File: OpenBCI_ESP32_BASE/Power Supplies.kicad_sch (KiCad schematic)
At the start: 32 parts, among them J1 Conn_01x02, J2 Conn_02x03_Odd_Even, J3 Conn_02x02_Odd_Even, SW1 SW_SPDT, U10 TPS72325, U8 TPS60403, U9 TPS73225

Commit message: Firmware updates
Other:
- moved on the sheet: C33
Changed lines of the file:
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@@
   (junction (at 72.39 91.44) (diameter 0) (color 0 0 0 0)
   )
-  (junction (at 27.94 58.42) (diameter 0) (color 0 0 0 0)
+  (junction (at 21.59 58.42) (diameter 0) (color 0 0 0 0)
   )
   (junction (at 110.49 104.14) (diameter 0) (color 0 0 0 0)
@@
     (stroke (width 0) (type default) (color 0 0 0 0))
   )
-  (wire (pts (xy 27.94 58.42) (xy 27.94 62.23))
+  (wire (pts (xy 21.59 58.42) (xy 21.59 62.23))
     (stroke (width 0) (type default) (color 0 0 0 0))
   )
@@
     (stroke (width 0) (type default) (color 0 0 0 0))
   )
-  (wire (pts (xy 27.94 58.42) (xy 38.1 58.42))
-    (stroke (width 0) (type default) (color 0 0 0 0))
-  )
   (wire (pts (xy 75.565 170.18) (xy 81.28 170.18))
     (stroke (width 0) (type default) (color 0 0 0 0))
@@
     (stroke (width 0) (type default) (color 0 0 0 0))
   )
-  (wire (pts (xy 27.94 52.07) (xy 27.94 58.42))
+  (wire (pts (xy 21.59 52.07) (xy 21.59 58.42))
     (stroke (width 0) (type default) (color 0 0 0 0))
   )
@@
     (stroke (width 0) (type default) (color 0 0 0 0))
   )
+  (wire (pts (xy 21.59 58.42) (xy 38.1 58.42))
+    (stroke (width 0) (type default) (color 0 0 0 0))
+  )
   (wire (pts (xy 80.01 132.08) (xy 80.01 128.27))
     (stroke (width 0) (type default) (color 0 0 0 0))
@@
     (stroke (width 0) (type default) (color 0 0 0 0))
   )
-  (wire (pts (xy 27.94 74.93) (xy 27.94 69.85))
+  (wire (pts (xy 21.59 74.93) (xy 21.59 69.85))
     (stroke (width 0) (type default) (color 0 0 0 0))
   )
@@
     (pin "5")
   )
-  (symbol (lib_id "Device:C") (at 27.94 66.04 0) (unit 1)
-    (in_bom yes) (on_board yes)
-    (property "Reference" "C33" (id 0) (at 30.861 64.8716 0)
-      (effects (font (size 1.27 1.27)) (justify left))
-    )
-    (property "Value" "10u" (id 1) (at 30.861 67.183 0)
-      (effects (font (size 1.27 1.27)) (justify left))
-    )
-    (property "Footprint" "Capacitor_SMD:C_0805_2012Metric" (id 2) (at 28.9052 69.85 0)
-      (effects (font (size 1.27 1.27)) hide)
-    )
-    (property "Datasheet" "~" (id 3) (at 27.94 66.04 0)
+  (symbol (lib_id "Device:C") (at 21.59 66.04 0) (unit 1)
+    (in_bom yes) (on_board yes)
+    (property "Reference" "C33" (id 0) (at 24.511 64.8716 0)
+      (effects (font (size 1.27 1.27)) (justify left))
+    )
+    (property "Value" "10u" (id 1) (at 24.511 67.183 0)
+      (effects (font (size 1.27 1.27)) (justify left))
+    )
+    (property "Footprint" "Capacitor_SMD:C_0805_2012Metric" (id 2) (at 22.5552 69.85 0)
+      (effects (font (size 1.27 1.27)) hide)
+    )
+    (property "Datasheet" "~" (id 3) (at 21.59 66.04 0)
       (effects (font (size 1.27 1.27)) hide)
     )
@@
     (pin "2")
   )
-  (symbol (lib_id "power:+5V") (at 27.94 52.07 0) (unit 1)
-    (in_bom yes) (on_board yes)
-    (property "Reference" "#PWR023" (id 0) (at 27.94 55.88 0)
-      (effects (font (size 1.27 1.27)) hide)
-    )
-    (property "Value" "+5V" (id 1) (at 28.321 47.6758 0))
-    (property "Footprint" "" (id 2) (at 27.94 52.07 0)
-      (effects (font (size 1.27 1.27)) hide)
-    )
-    (property "Datasheet" "" (id 3) (at 27.94 52.07 0)
+  (symbol (lib_id "power:+5V") (at 21.59 52.07 0) (unit 1)
+    (in_bom yes) (on_board yes)
+    (property "Reference" "#PWR023" (id 0) (at 21.59 55.88 0)
+      (effects (font (size 1.27 1.27)) hide)
+    )
+    (property "Value" "+5V" (id 1) (at 21.971 47.6758 0))
+    (property "Footprint" "" (id 2) (at 21.59 52.07 0)
+      (effects (font (size 1.27 1.27)) hide)
+    )
+    (property "Datasheet" "" (id 3) (at 21.59 52.07 0)
       (effects (font (size 1.27 1.27)) hide)
     )
@@
     (pin "6")
   )
-  (symbol (lib_id "power:GND") (at 27.94 74.93 0) (unit 1)
-    (in_bom yes) (on_board yes)
-    (property "Reference" "#PWR024" (id 0) (at 27.94 81.28 0)
-      (effects (font (size 1.27 1.27)) hide)
-    )
-    (property "Value" "GND" (id 1) (at 28.067 79.3242 0))
-    (property "Footprint" "" (id 2) (at 27.94 74.93 0)
-      (effects (font (size 1.27 1.27)) hide)
-    )
-    (property "Datasheet" "" (id 3) (at 27.94 74.93 0)
-      (effects (font (size 1.27 1.27)) hide)
-    )
+  (symbol (lib_id "power:GND") (at 21.59 74.93 0) (unit 1)
+    (in_bom yes) (on_board yes)
+    (property "Reference" "#PWR024" (id 0) (at 21.59 81.28 0)
+      (effects (font (size 1.27 1.27)) hide)
+    )
+    (property "Value" "GND" (id 1) (at 21.717 79.3242 0))
+    (property "Footprint" "" (id 2) (at 21.59 74.93 0)
+      (effects (font (size 1.27 1.27)) hide)
+    )
+    (property "Datasheet" "" (id 3) (at 21.59 74.93 0)
+      (effects (font (size 1.27 1.27)) hide)
+    )

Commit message: Code and STL updates
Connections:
- net +2V5: now also J2.2 (Pin_2), J2.4 (Pin_4); no longer J2.1 (Pin_1), J2.3 (Pin_3)
- net -2V5: now also J3.2 (Pin_2), J3.4 (Pin_4); no longer J3.1 (Pin_1), J3.3 (Pin_3)
- net GND: now also J2.1 (Pin_1), J2.3 (Pin_3), J2.5 (Pin_5), J3.1 (Pin_1), J3.3 (Pin_3); no longer J2.2 (Pin_2), J2.4 (Pin_4), J2.6 (Pin_6), J3.2 (Pin_2), J3.4 (Pin_4)
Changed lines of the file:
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@@
 (kicad_sch (version 20211123) (generator eeschema)
   (paper "A4")
+  (junction (at 207.01 128.27) (diameter 0) (color 0 0 0 0)
+  )
   (junction (at 124.46 58.42) (diameter 0) (color 0 0 0 0)
   )
@@
   )
   (junction (at 72.39 128.27) (diameter 0) (color 0 0 0 0)
-  )
-  (junction (at 207.01 128.27) (diameter 0) (color 0 0 0 0)
   )
   (junction (at 166.37 128.27) (diameter 0) (color 0 0 0 0)
@@
     (stroke (width 0) (type default) (color 0 0 0 0))
   )
+  (wire (pts (xy 223.52 128.27) (xy 226.06 128.27))
+    (stroke (width 0) (type default) (color 0 0 0 0))
+  )
   (wire (pts (xy 223.52 91.44) (xy 226.06 91.44))
     (stroke (width 0) (type default) (color 0 0 0 0))
@@
     (stroke (width 0) (type default) (color 0 0 0 0))
   )
-  (wire (pts (xy 223.52 128.27) (xy 226.06 128.27))
-    (stroke (width 0) (type default) (color 0 0 0 0))
-  )
   (wire (pts (xy 81.28 91.44) (xy 72.39 91.44))
     (stroke (width 0) (type default) (color 0 0 0 0))
@@
     (stroke (width 0) (type default) (color 0 0 0 0))
   )
-  (wire (pts (xy 210.82 128.27) (xy 207.01 128.27))
-    (stroke (width 0) (type default) (color 0 0 0 0))
-  )
   (wire (pts (xy 109.855 167.64) (xy 109.855 166.37))
     (stroke (width 0) (type default) (color 0 0 0 0))
@@
   )
   (wire (pts (xy 72.39 130.81) (xy 72.39 128.27))
+    (stroke (width 0) (type default) (color 0 0 0 0))
+  )
+  (wire (pts (xy 207.01 128.27) (xy 210.82 128.27))
     (stroke (width 0) (type default) (color 0 0 0 0))
   )
@@
     (pin "1")
   )
-  (symbol (lib_id "Connector_Generic:Conn_02x02_Odd_Even") (at 215.9 128.27 0) (unit 1)
+  (symbol (lib_id "Connector_Generic:Conn_02x02_Odd_Even") (at 218.44 128.27 0) (mirror y) (unit 1)
     (in_bom yes) (on_board yes)
     (property "Reference" "J3" (id 0) (at 217.17 122.7582 0))
     (property "Value" "Conn_02x02_Odd_Even" (id 1) (at 217.17 125.0696 0))
-    (property "Footprint" "OpenBCI_ESP32:PinHeaderReverse_2x02_P2.54mml_OpenBCI" (id 2) (at 215.9 128.27 0)
-      (effects (font (size 1.27 1.27)) hide)
-    )
-    (property "Datasheet" "~" (id 3) (at 215.9 128.27 0)
+    (property "Footprint" "OpenBCI_ESP32:PinHeaderReverse_2x02_P2.54mml_OpenBCI" (id 2) (at 218.44 128.27 0)
+      (effects (font (size 1.27 1.27)) hide)
+    )
+    (property "Datasheet" "~" (id 3) (at 218.44 128.27 0)
       (effects (font (size 1.27 1.27)) hide)
     )
@@
     (pin "1")
   )
-  (symbol (lib_id "Connector_Generic:Conn_02x03_Odd_Even") (at 215.9 93.98 0) (unit 1)
+  (symbol (lib_id "Connector_Generic:Conn_02x03_Odd_Even") (at 218.44 93.98 0) (mirror y) (unit 1)
     (in_bom yes) (on_board yes)
     (property "Reference" "J2" (id 0) (at 217.17 85.9282 0))
     (property "Value" "Conn_02x03_Odd_Even" (id 1) (at 217.17 88.2396 0))
-    (property "Footprint" "OpenBCI_ESP32:PinHeaderReverse_2x03_P2.54mm_OpenBCI" (id 2) (at 215.9 93.98 0)
-      (effects (font (size 1.27 1.27)) hide)
-    )
-    (property "Datasheet" "~" (id 3) (at 215.9 93.98 0)
-      (effects (font (size 1.27 1.27)) hide)
-    )
+    (property "Footprint" "OpenBCI_ESP32:PinHeaderReverse_2x03_P2.54mm_OpenBCI" (id 2) (at 218.44 93.98 0)
+      (effects (font (size 1.27 1.27)) hide)
+    )
+    (property "Datasheet" "~" (id 3) (at 218.44 93.98 0)
+      (effects (font (size 1.27 1.27)) hide)
+    )

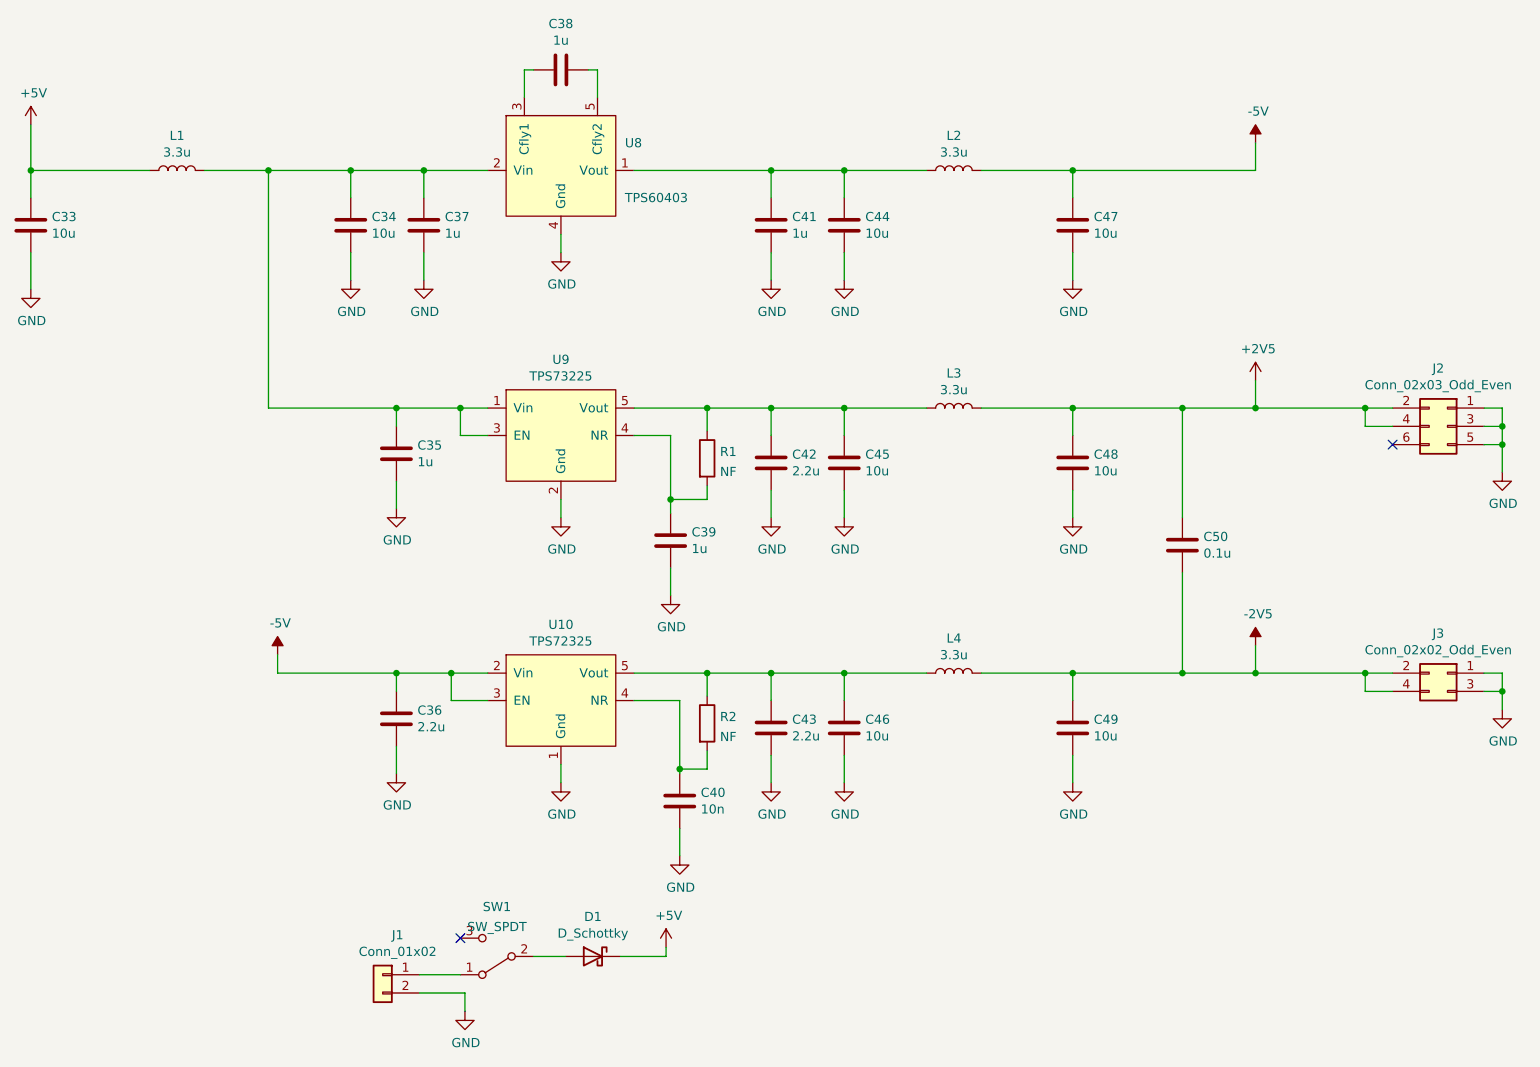
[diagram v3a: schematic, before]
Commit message: add ADS1298 files
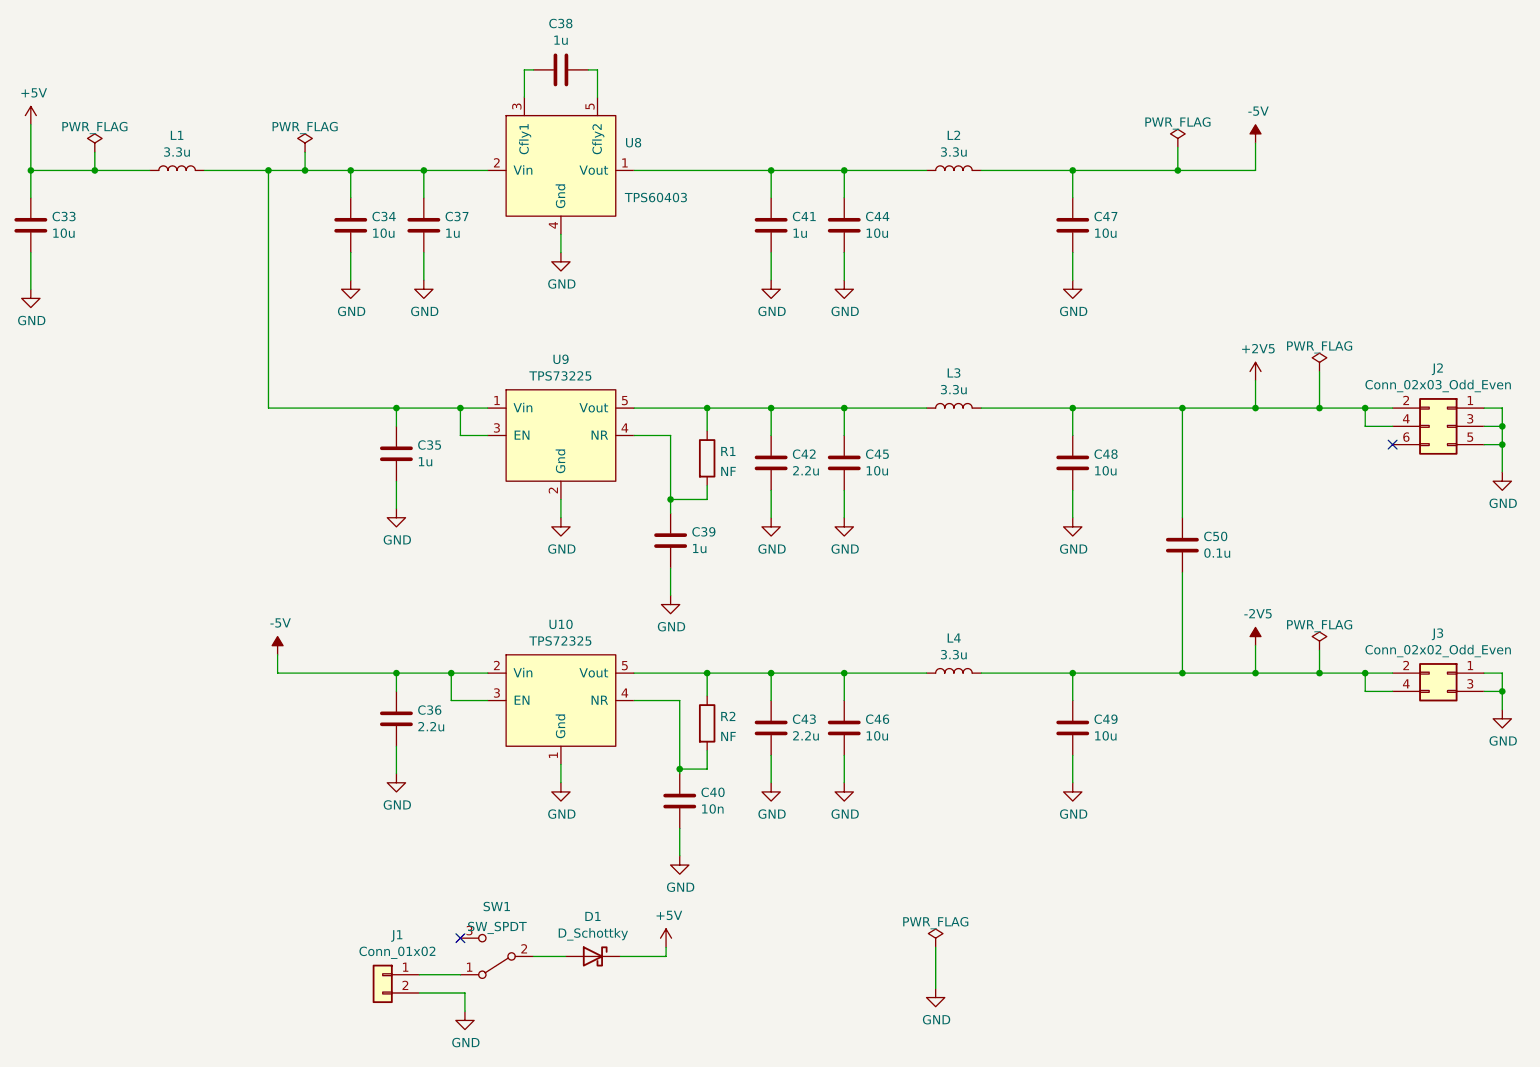
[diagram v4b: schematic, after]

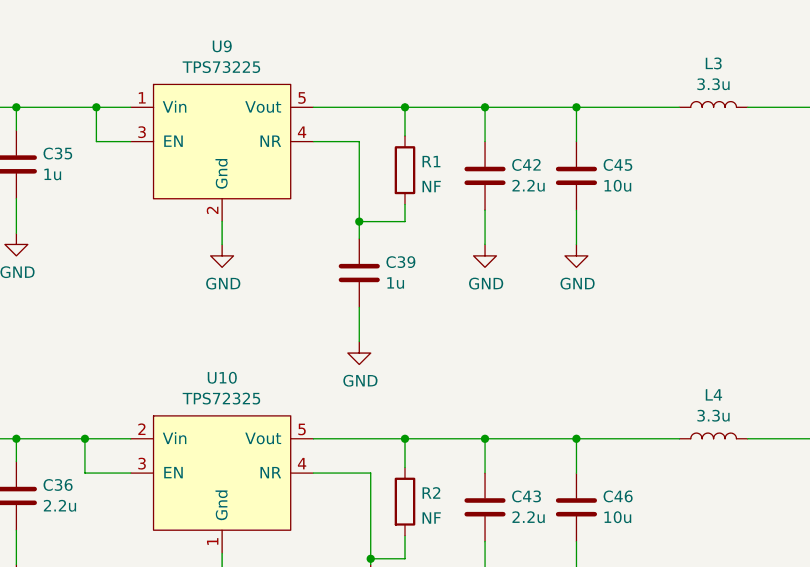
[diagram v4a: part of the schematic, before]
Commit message: Fix ADS1298 Mounting Holes
Fix ADS1298R Mounting holes shorting layers
Add some ADS1298R Arduino Files
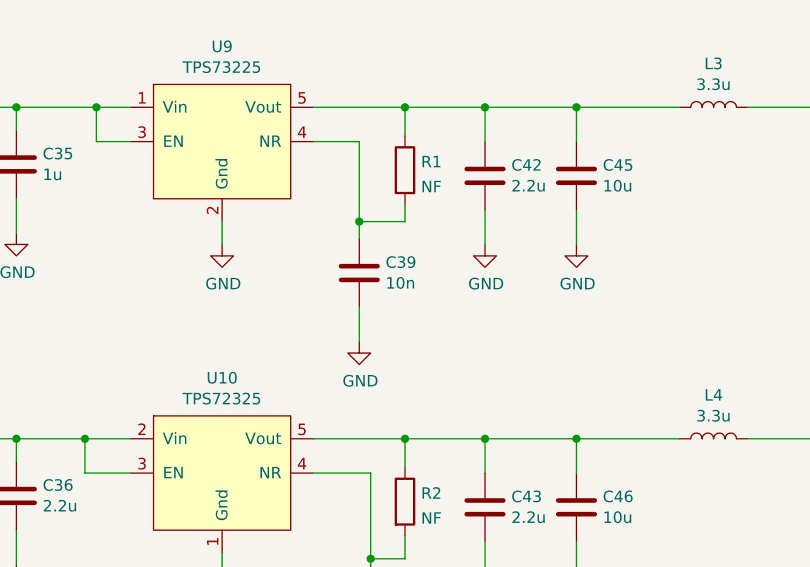
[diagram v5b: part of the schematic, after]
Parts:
- C39: value 1u -> 10n
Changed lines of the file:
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@@
       (effects (font (size 1.27 1.27)) (justify left))
     )
-    (property "Value" "1u" (at 113.411 110.998 0)
+    (property "Value" "10n" (at 113.411 110.998 0)
       (effects (font (size 1.27 1.27)) (justify left))
     )
